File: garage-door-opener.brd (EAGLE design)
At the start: 54.3 x 47.6 mm, 17 parts, among them IC1 LM2575-3.3T, K1 RR1A, T1 BC547, U1 ESP8266, X2 Connector

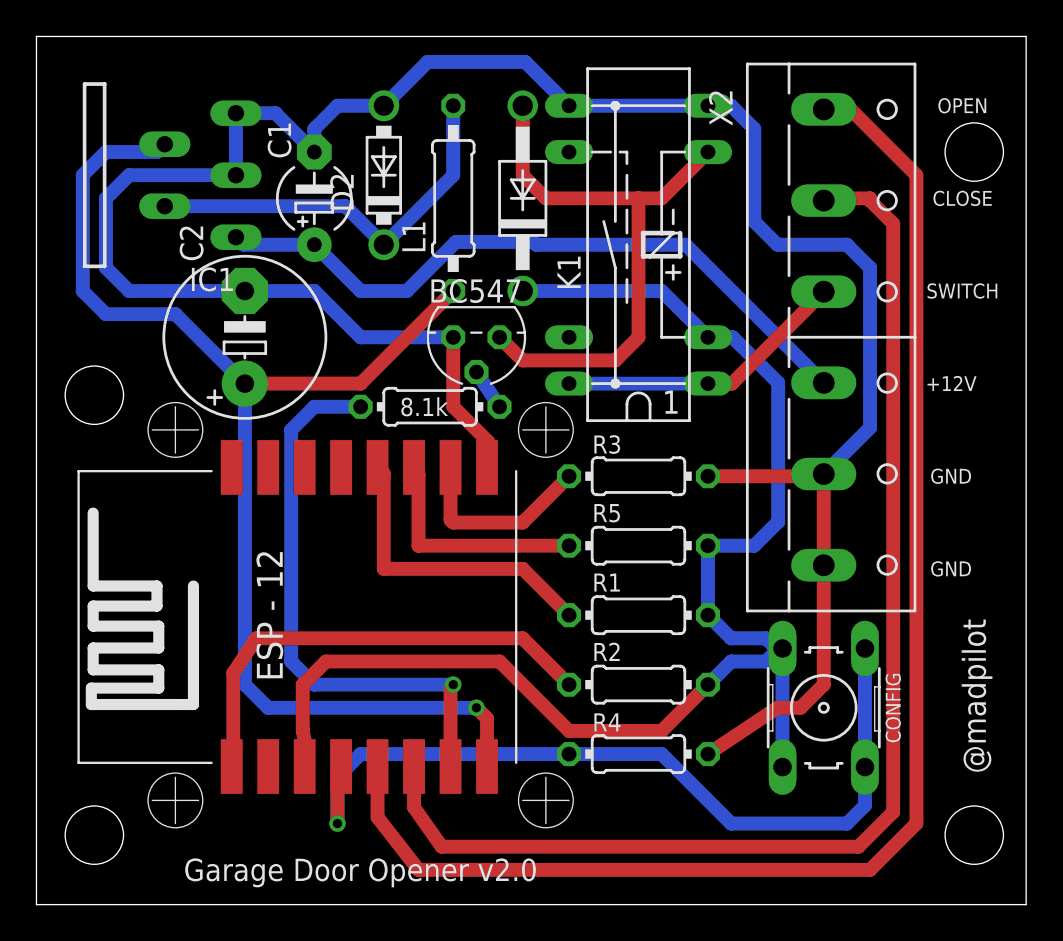
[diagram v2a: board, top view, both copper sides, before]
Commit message: Removing another via by rotating a resistor. They no longer ligne up, but one less via is a win, right?
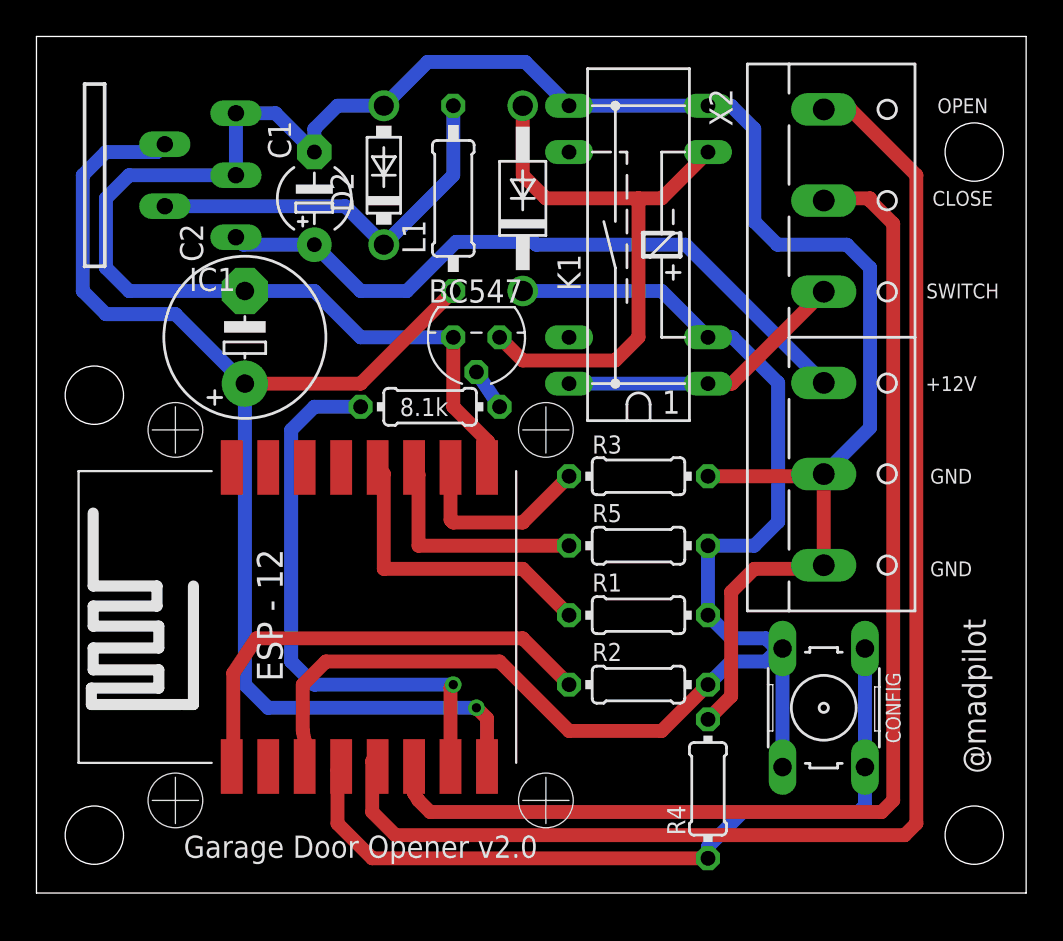
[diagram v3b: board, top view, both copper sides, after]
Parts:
- moved R4 4.26 mm to (36.8, 42.5), turned to 270 degrees
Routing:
- net N$12: track 45.8 -> 43.1 mm, vias 1 -> 0
- net N$10: track 67.2 -> 64.6 mm
- net GND: track 127.5 -> 126.5 mm
- net N$11: track 76.9 -> 76.0 mm
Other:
- board size 54.3 x 47.6 mm -> 54.3 x 47 mm
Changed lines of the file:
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@@
 <board>
 <plain>
-<wire x1="0" y1="36.195" x2="54.28" y2="36.195" width="0" layer="20"/>
-<wire x1="54.28" y1="36.195" x2="54.28" y2="83.81" width="0" layer="20"/>
+<wire x1="0" y1="36.83" x2="54.28" y2="36.83" width="0" layer="20"/>
+<wire x1="54.28" y1="36.83" x2="54.28" y2="83.81" width="0" layer="20"/>
 <wire x1="54.28" y1="83.81" x2="0" y2="83.81" width="0" layer="20"/>
-<wire x1="0" y1="83.81" x2="0" y2="36.195" width="0" layer="20"/>
+<wire x1="0" y1="83.81" x2="0" y2="36.83" width="0" layer="20"/>
 <text x="50.165" y="64.77" size="0.8128" layer="21" font="vector" ratio="5" align="center">+12V</text>
 <text x="50.165" y="59.69" size="0.8128" layer="21" font="vector" ratio="5" align="center">GND</text>
@@
 <text x="50.8" y="74.93" size="0.8128" layer="21" ratio="5" align="center">CLOSE</text>
 <text x="50.8" y="69.85" size="0.8128" layer="21" font="vector" ratio="5" align="center">SWITCH</text>
-<text x="17.78" y="38.1" size="1.2192" layer="21" font="vector" ratio="5" align="center">Garage Door Opener v2.0</text>
+<text x="17.78" y="39.37" size="1.2192" layer="21" font="vector" ratio="5" align="center">Garage Door Opener v2.0</text>
 <text x="51.435" y="47.625" size="1.27" layer="21" font="vector" ratio="5" rot="R90" align="center">@madpilot</text>
 <hole x="3.175" y="40.005" drill="3.2"/>
@@
 <attribute name="OC_NEWARK" value="36M3542" x="43.18" y="46.99" size="0.6096" layer="27" rot="R90" display="off"/>
 </element>
-<element name="R4" library="resistor" library_urn="urn:adsk.eagle:library:348" package="0204/7" package3d_urn="urn:adsk.eagle:package:25945/1" value="3k3" x="33.02" y="44.45" smashed="yes" rot="R180">
-<attribute name="NAME" x="30.48" y="45.6946" size="0.9906" layer="25" ratio="10" rot="R180" align="top-right"/>
-<attribute name="VALUE" x="34.6456" y="44.9326" size="0.9906" layer="27" ratio="10" rot="R180"/>
+<element name="R4" library="resistor" library_urn="urn:adsk.eagle:library:348" package="0204/7" package3d_urn="urn:adsk.eagle:package:25945/1" value="3k3" x="36.83" y="42.545" smashed="yes" rot="R270">
+<attribute name="NAME" x="35.5854" y="40.005" size="0.9906" layer="25" ratio="10" rot="R270" align="top-right"/>
+<attribute name="VALUE" x="36.3474" y="44.1706" size="0.9906" layer="27" ratio="10" rot="R270"/>
 </element>
 <element name="R5" library="resistor" library_urn="urn:adsk.eagle:library:348" package="0204/7" package3d_urn="urn:adsk.eagle:package:25945/1" value="3k3" x="33.02" y="55.88" smashed="yes">
@@
 <wire x1="17.78" y1="67.31" x2="22.86" y2="67.31" width="0.762" layer="16"/>
 <wire x1="36.83" y1="59.69" x2="43.18" y2="59.69" width="0.762" layer="1"/>
-<wire x1="36.83" y1="44.45" x2="40.64" y2="46.99" width="0.762" layer="1"/>
-<wire x1="40.64" y1="46.99" x2="41.91" y2="46.99" width="0.762" layer="1"/>
-<wire x1="41.91" y1="46.99" x2="43.18" y2="48.26" width="0.762" layer="1"/>
-<wire x1="43.18" y1="48.26" x2="43.18" y2="54.81" width="0.762" layer="1"/>
 <wire x1="43.18" y1="59.81" x2="45.72" y2="62.35" width="0.762" layer="16"/>
 <wire x1="45.72" y1="71.12" x2="44.45" y2="72.39" width="0.762" layer="16"/>
@@
 <wire x1="24.765" y1="61.595" x2="24.765" y2="60.225" width="0.762" layer="1"/>
 <wire x1="24.765" y1="60.225" x2="24.71" y2="60.17" width="0.762" layer="1"/>
+<wire x1="36.83" y1="46.355" x2="38.1" y2="47.625" width="0.762" layer="1"/>
+<wire x1="38.1" y1="47.625" x2="38.1" y2="53.34" width="0.762" layer="1"/>
+<wire x1="38.1" y1="53.34" x2="39.37" y2="54.61" width="0.762" layer="1"/>
+<wire x1="42.98" y1="54.61" x2="43.18" y2="54.81" width="0.762" layer="1"/>
+<wire x1="39.37" y1="54.61" x2="42.98" y2="54.61" width="0.762" layer="1"/>
 </signal>
 <signal name="VCC">
@@
 <contactref element="X2" pad="2"/>
 <contactref element="U1" pad="GPIO12"/>
-<wire x1="20.71" y1="43.77" x2="20.71" y2="41.52" width="0.762" layer="1"/>
-<wire x1="20.71" y1="41.52" x2="22.225" y2="39.37" width="0.762" layer="1"/>
-<wire x1="22.225" y1="39.37" x2="45.085" y2="39.37" width="0.762" layer="1"/>
-<wire x1="45.085" y1="39.37" x2="46.99" y2="41.275" width="0.762" layer="1"/>
-<wire x1="46.99" y1="41.275" x2="46.99" y2="73.54" width="0.762" layer="1"/>
+<wire x1="46.99" y1="41.91" x2="46.99" y2="73.54" width="0.762" layer="1"/>
 <wire x1="46.99" y1="73.54" x2="45.72" y2="74.81" width="0.762" layer="1"/>
 <wire x1="45.72" y1="74.81" x2="45.72" y2="74.93" width="0.762" layer="1"/>
 <wire x1="45.72" y1="74.93" x2="43.3" y2="74.93" width="0.762" layer="1"/>
 <wire x1="43.3" y1="74.93" x2="43.18" y2="74.81" width="0.762" layer="1"/>
+<wire x1="46.99" y1="41.91" x2="46.355" y2="41.275" width="0.762" layer="1"/>
+<wire x1="46.355" y1="41.275" x2="21.59" y2="41.275" width="0.762" layer="1"/>
+<wire x1="21.59" y1="41.275" x2="20.955" y2="41.91" width="0.762" layer="1"/>
+<wire x1="20.955" y1="41.91" x2="20.71" y2="42.3" width="0.762" layer="1"/>
+<wire x1="20.71" y1="42.3" x2="20.71" y2="43.77" width="0.762" layer="1"/>
 </signal>
 <signal name="N$11">
 <contactref element="X2" pad="1"/>
 <contactref element="U1" pad="GPIO14"/>
-<wire x1="18.71" y1="43.77" x2="18.71" y2="40.98" width="0.762" layer="1"/>
-<wire x1="18.71" y1="40.98" x2="20.955" y2="38.1" width="0.762" layer="1"/>
-<wire x1="20.955" y1="38.1" x2="45.72" y2="38.1" width="0.762" layer="1"/>
-<wire x1="45.72" y1="38.1" x2="48.26" y2="40.64" width="0.762" layer="1"/>
 <wire x1="48.26" y1="76.2" x2="44.65" y2="79.81" width="0.762" layer="1"/>
 <wire x1="44.65" y1="79.81" x2="43.18" y2="79.81" width="0.762" layer="1"/>
-<wire x1="48.26" y1="40.64" x2="48.26" y2="76.2" width="0.762" layer="1"/>
+<wire x1="48.26" y1="76.2" x2="48.26" y2="40.64" width="0.762" layer="1"/>
+<wire x1="48.26" y1="40.64" x2="47.625" y2="40.005" width="0.762" layer="1"/>
+<wire x1="47.625" y1="40.005" x2="19.685" y2="40.005" width="0.762" layer="1"/>
+<wire x1="19.685" y1="40.005" x2="18.415" y2="41.275" width="0.762" layer="1"/>
+<wire x1="18.415" y1="44.065" x2="18.71" y2="43.77" width="0.762" layer="1"/>
+<wire x1="18.415" y1="41.275" x2="18.415" y2="44.065" width="0.762" layer="1"/>
 </signal>
 <signal name="N$12">
@@
 <contactref element="R4" pad="2"/>
 <wire x1="45.4406" y1="43.7388" x2="45.4406" y2="41.6306" width="0.762" layer="16"/>
-<wire x1="44.45" y1="40.64" x2="45.4406" y2="41.6306" width="0.762" layer="16"/>
-<via x="16.51" y="40.64" extent="1-16" drill="0.508"/>
+<wire x1="45.085" y1="41.275" x2="45.4406" y2="41.6306" width="0.762" layer="16"/>
+<wire x1="45.4406" y1="50.2412" x2="45.4406" y2="43.7388" width="0.762" layer="16"/>
+<wire x1="45.085" y1="41.275" x2="38.735" y2="41.275" width="0.762" layer="16"/>
+<wire x1="38.735" y1="41.275" x2="36.83" y2="39.37" width="0.762" layer="16"/>
+<wire x1="36.83" y1="39.37" x2="36.83" y2="38.735" width="0.762" layer="16"/>
+<wire x1="36.83" y1="38.735" x2="18.415" y2="38.735" width="0.762" layer="1"/>
+<wire x1="18.415" y1="38.735" x2="16.51" y2="40.64" width="0.762" layer="1"/>
+<wire x1="16.51" y1="43.57" x2="16.71" y2="43.77" width="0.762" layer="1"/>
 <wire x1="16.51" y1="40.64" x2="16.51" y2="43.57" width="0.762" layer="1"/>
-<wire x1="16.51" y1="43.57" x2="16.71" y2="43.77" width="0.762" layer="1"/>
-<wire x1="45.4406" y1="50.2412" x2="45.4406" y2="43.7388" width="0.762" layer="16"/>
-<wire x1="29.21" y1="44.45" x2="34.29" y2="44.45" width="0.762" layer="16"/>
-<wire x1="34.29" y1="44.45" x2="38.1" y2="40.64" width="0.762" layer="16"/>
-<wire x1="38.1" y1="40.64" x2="44.45" y2="40.64" width="0.762" layer="16"/>
-<wire x1="17.78" y1="44.45" x2="16.51" y2="43.18" width="0.762" layer="16"/>
-<wire x1="16.51" y1="43.18" x2="16.51" y2="40.64" width="0.762" layer="16"/>
-<wire x1="29.21" y1="44.45" x2="17.78" y2="44.45" width="0.762" layer="16"/>
 </signal>
 <signal name="N$6">

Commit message: removed all the vias. Re-routed some tracks around the developer holes (sort of)
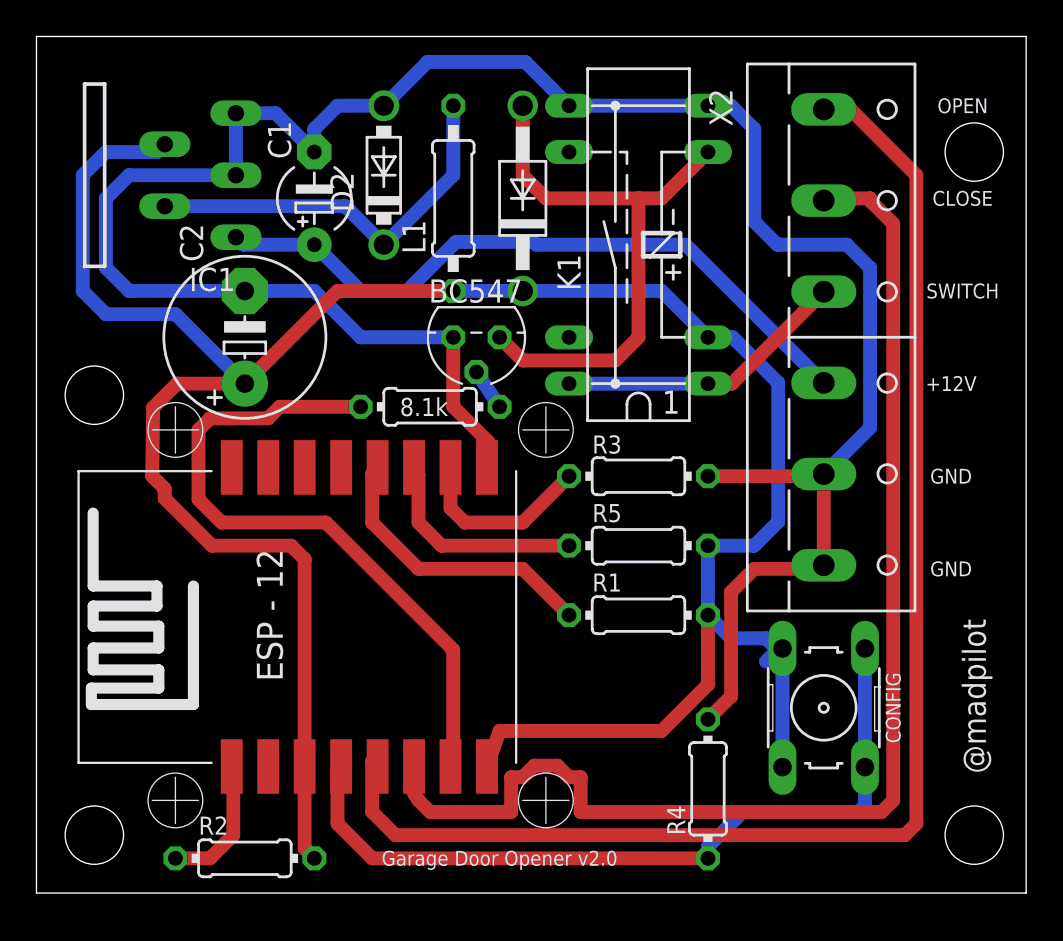
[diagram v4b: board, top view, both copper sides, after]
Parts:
- moved R2 23.6 mm to (11.4, 38.7)
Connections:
- removed net N$4: C2.+, IC1.4, L1.1, U1.VCC
- net VCC: now also C2.+, IC1.4, L1.1, U1.VCC
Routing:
- net N$4: track 69.3 -> 0.00 mm, vias 1 -> 0
- net VCC: track 78.1 -> 139.3 mm
- net N$8: track 25.7 -> 7.50 mm
- net N$9: track 31.0 -> 37.1 mm, vias 1 -> 0
- net N$10: track 64.6 -> 69.0 mm
- net N$7: track 16.9 -> 16.0 mm
- net N$13: track 12.6 -> 11.9 mm
